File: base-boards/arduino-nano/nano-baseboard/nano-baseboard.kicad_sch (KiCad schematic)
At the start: 3 parts, among them J1 Conn_02x15_Odd_Even, J2 Conn_02x15_Odd_Even

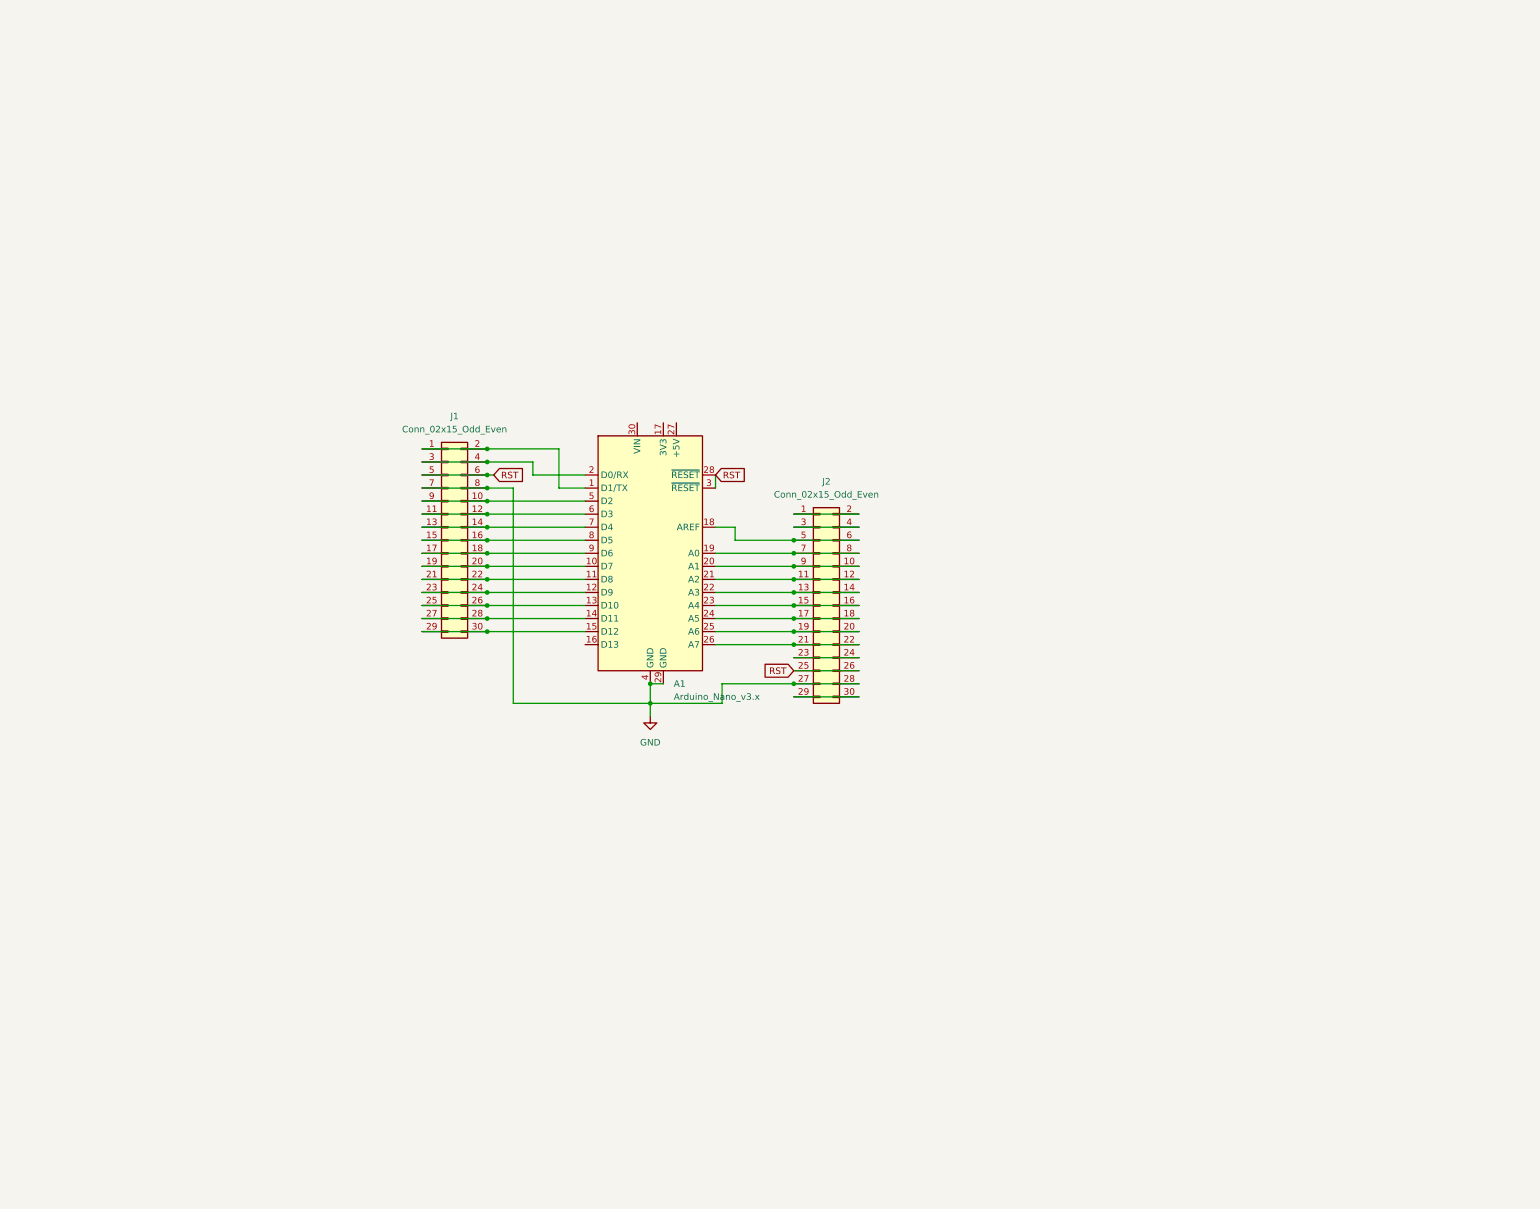
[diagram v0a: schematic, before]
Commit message: Added Arduino Nano breakout
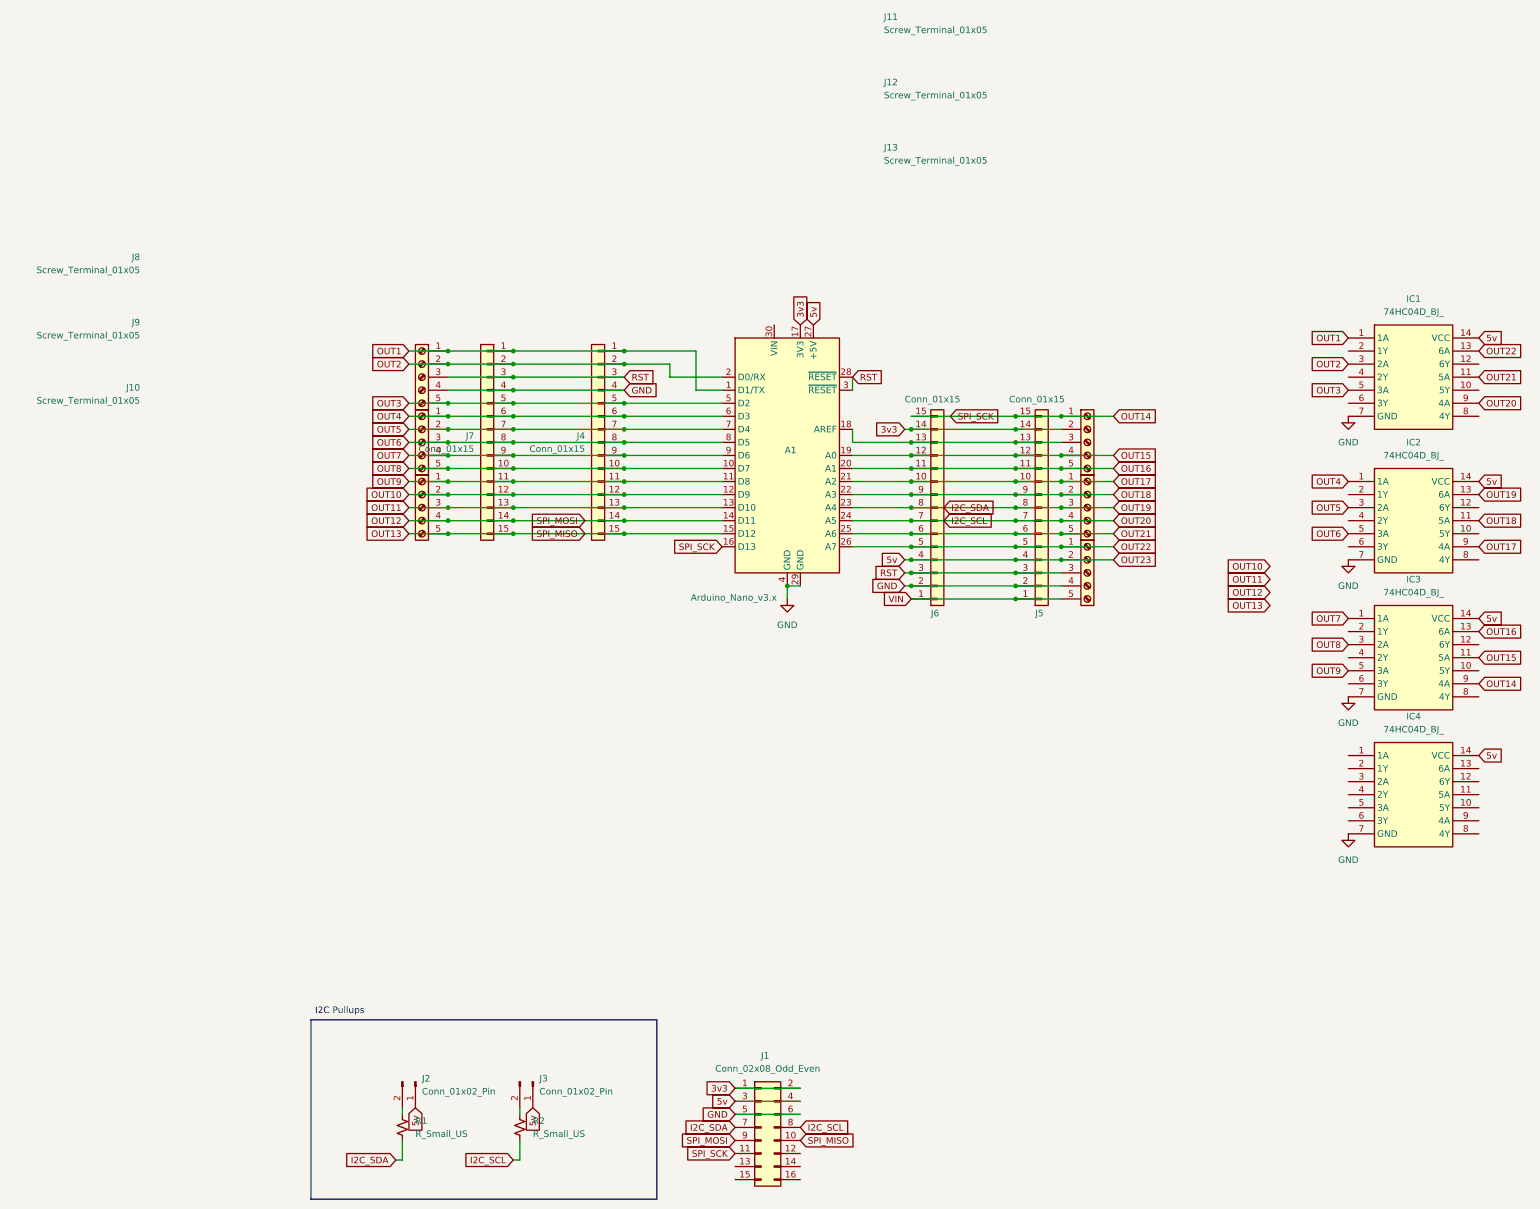
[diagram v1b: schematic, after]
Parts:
- removed J1, J2: Conn_02x15_Odd_Even, Connector_PinHeader_2.54mm:PinHeader_2x15_P2.54mm_Vertical, symbol Connector_Generic:Conn_02x15_Odd_Even
- added IC1, IC2, IC3, IC4: 74HC04D_BJ_, Package_SO:SOIC-14_3.9x8.7mm_P1.27mm, symbol 74HC04D_BJ_:74HC04D_BJ_
- added J1: Conn_02x08_Odd_Even, Connector_PinHeader_2.54mm:PinHeader_2x08_P2.54mm_Vertical, symbol Connector_Generic:Conn_02x08_Odd_Even
- added J10, J11, J12, J13, J8, J9: Screw_Terminal_01x05, TerminalBlock_Phoenix:TerminalBlock_Phoenix_MKDS-1,5-5-5.08_1x05_P5.08mm_Horizontal, symbol Connector:Screw_Terminal_01x05
- added J2, J3: Conn_01x02_Pin, Connector_PinHeader_2.54mm:PinHeader_1x02_P2.54mm_Vertical, symbol Connector:Conn_01x02_Pin
- added J4, J5, J6, J7: Conn_01x15, Connector_PinHeader_2.54mm:PinHeader_1x15_P2.54mm_Vertical, symbol Connector_Generic:Conn_01x15
- added R1, R2: R_Small_US, Resistor_SMD:R_0603_1608Metric, symbol Device:R_Small_US
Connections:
- net GND: now also IC1.7 (GND), IC2.7 (GND), IC3.7 (GND), IC4.7 (GND), J1.5 (Pin_5), J1.6 (Pin_6), J13.4 (Pin_4), J4.4 (Pin_4), J5.2 (Pin_2), J6.2 (Pin_2), J7.4 (Pin_4), J8.4 (Pin_4)
- net RST: now also J13.3 (Pin_3), J4.3 (Pin_3), J5.3 (Pin_3), J6.3 (Pin_3), J7.3 (Pin_3), J8.3 (Pin_3)
- net OUT1: now reaches A1.1 (D1/TX)
- net OUT1: now also IC1.1 (1A), J4.1 (Pin_1), J7.1 (Pin_1), J8.1 (Pin_1)
- net OUT3: now reaches A1.5 (D2)
- net OUT3: now also IC1.5 (3A), J4.5 (Pin_5), J7.5 (Pin_5), J8.5 (Pin_5)
- net OUT4: now reaches A1.6 (D3)
- net OUT4: now also IC2.1 (1A), J4.6 (Pin_6), J7.6 (Pin_6), J9.1 (Pin_1)
- net OUT5: now reaches A1.7 (D4)
- net OUT5: now also IC2.3 (2A), J4.7 (Pin_7), J7.7 (Pin_7), J9.2 (Pin_2)
- net OUT6: now reaches A1.8 (D5)
- net OUT6: now also IC2.5 (3A), J4.8 (Pin_8), J7.8 (Pin_8), J9.3 (Pin_3)
- net OUT7: now reaches A1.9 (D6)
- net OUT7: now also IC3.1 (1A), J4.9 (Pin_9), J7.9 (Pin_9), J9.4 (Pin_4)
- net OUT8: now reaches A1.10 (D7)
- net OUT8: now also IC3.3 (2A), J4.10 (Pin_10), J7.10 (Pin_10), J9.5 (Pin_5)
- net OUT9: now reaches A1.11 (D8)
- net OUT9: now also IC3.5 (3A), J10.1 (Pin_1), J4.11 (Pin_11), J7.11 (Pin_11)
- net OUT10: now reaches A1.12 (D9)
- net OUT10: now also J10.2 (Pin_2), J4.12 (Pin_12), J7.12 (Pin_12)
- net OUT11: now reaches A1.13 (D10)
- net OUT11: now also J10.3 (Pin_3), J4.13 (Pin_13), J7.13 (Pin_13)
- net OUT12: now reaches A1.14 (D11)
- net OUT12: now also J1.9 (Pin_9), J10.4 (Pin_4), J4.14 (Pin_14), J7.14 (Pin_14)
- net OUT13: now reaches A1.15 (D12)
- net OUT13: now also J1.10 (Pin_10), J10.5 (Pin_5), J4.15 (Pin_15), J7.15 (Pin_15)
- net OUT2: now reaches A1.2 (D0/RX)
- net OUT2: now also IC1.3 (2A), J4.2 (Pin_2), J7.2 (Pin_2), J8.2 (Pin_2)
- net OUT14: now reaches A1.16 (D13)
- net OUT14: now also IC3.9 (4A), J1.11 (Pin_11), J11.1 (Pin_1), J5.15 (Pin_15), J6.15 (Pin_15)
- net 3v3: now reaches A1.17 (3V3)
- net 3v3: now also J1.1 (Pin_1), J1.2 (Pin_2), J11.2 (Pin_2), J5.14 (Pin_14), J6.14 (Pin_14)
- net at A1.18 (AREF): now also J11.3 (Pin_3), J5.13 (Pin_13), J6.13 (Pin_13)
- net OUT15: now reaches A1.19 (A0)
- net OUT15: now also IC3.11 (5A), J11.4 (Pin_4), J5.12 (Pin_12), J6.12 (Pin_12)
- net OUT16: now reaches A1.20 (A1)
- net OUT16: now also IC3.13 (6A), J11.5 (Pin_5), J5.11 (Pin_11), J6.11 (Pin_11)
- net OUT17: now reaches A1.21 (A2)
- net OUT17: now also IC2.9 (4A), J12.1 (Pin_1), J5.10 (Pin_10), J6.10 (Pin_10)
- net OUT18: now reaches A1.22 (A3)
- net OUT18: now also IC2.11 (5A), J12.2 (Pin_2), J5.9 (Pin_9), J6.9 (Pin_9)
- net I2C_SDA: now reaches A1.23 (A4)
- net I2C_SDA: now also IC2.13 (6A), J1.7 (Pin_7), J12.3 (Pin_3), J5.8 (Pin_8), J6.8 (Pin_8), R1.2
- net I2C_SCL: now reaches A1.24 (A5)
- net I2C_SCL: now also IC1.9 (4A), J1.8 (Pin_8), J12.4 (Pin_4), J5.7 (Pin_7), J6.7 (Pin_7), R2.2
- net OUT21: now reaches A1.25 (A6)
- net OUT21: now also IC1.11 (5A), J12.5 (Pin_5), J5.6 (Pin_6), J6.6 (Pin_6)
- net OUT22: now reaches A1.26 (A7)
- net OUT22: now also IC1.13 (6A), J13.1 (Pin_1), J5.5 (Pin_5), J6.5 (Pin_5)
- net 5v: now reaches A1.27 (+5V)
- net 5v: now also IC1.14 (VCC), IC2.14 (VCC), IC3.14 (VCC), IC4.14 (VCC), J1.3 (Pin_3), J1.4 (Pin_4), J13.2 (Pin_2), J2.1 (Pin_1), J3.1 (Pin_1), J5.4 (Pin_4), J6.4 (Pin_4)
- new net: J3.2 (Pin_2), R2.1
- new net: J2.2 (Pin_2), R1.1
- new net VIN: J13.5 (Pin_5), J5.1 (Pin_1), J6.1 (Pin_1)
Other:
- note added: "I2C Pullups"
- moved on the sheet: A1
